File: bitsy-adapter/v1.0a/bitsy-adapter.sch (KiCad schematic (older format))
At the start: 17 parts, among them J1 PMOD1A, J2 PMOD1A, J3 PMOD1A, J4 5V AUX, J5 5V AUX, J6 5V AUX

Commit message: Finish bitsy-adapter v1.0a
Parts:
- removed J5: 5V AUX, Connector_PinSocket_2.54mm:PinSocket_2x01_P2.54mm_Vertical, symbol Connector_Generic:Conn_02x01
- added J6: IO3, pkl_pin_headers:Pin_Header_Straight_Round_1x01, symbol Connector_Generic:Conn_01x01
- added J7: IO2, pkl_pin_headers:Pin_Header_Straight_Round_1x01, symbol Connector_Generic:Conn_01x01
- added LOGO1: 1BitSquared, pkl_logos:1b2_Logo_SilkS_4mm, symbol pkl_logos:1BitSquared
- renumbered J6 to J5
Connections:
- net labels added: IO2, IO3
- wire segments 100 -> 102
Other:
- moved on the sheet: H1, H2, H3, H4, J1, J2, J3, J4, J5, R1A, R1B, R1C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

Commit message: Change bitsy adapter pinout
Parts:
- J2: value PMOD1A -> PMOD1B
- J3: value PMOD1A -> PMOD2
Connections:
- net labels added: P0, P1, P10, P11, P12, P13, P14, P15, P16, P17, P18, P19, P2, P20, P21, P22, P23, P3, P4, P5, P6, P7, P8, P9
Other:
- moved on the sheet: R1A, R1B, R1C, R1D, R2A, R2B, R2C, R2D, R3A, R3B, R3C, R3D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

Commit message: Bitsy Adapter: Remove unused IO2 & IO3 pins
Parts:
- removed J6: IO3, pkl_pin_headers:Pin_Header_Straight_Round_1x01, symbol Connector_Generic:Conn_01x01
- removed J7: IO2, pkl_pin_headers:Pin_Header_Straight_Round_1x01, symbol Connector_Generic:Conn_01x01
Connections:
- net labels removed: IO2, IO3
- wire segments 102 -> 100
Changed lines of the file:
@@
 $EndComp
-$Comp
-L Connector_Generic:Conn_01x01 J6
-U 1 1 5F3ED57C
-P 5800 5000
-F 0 "J6" H 5880 5042 50  0000 L CNN
-F 1 "IO3" H 5880 4951 50  0000 L CNN
-F 2 "pkl_pin_headers:Pin_Header_Straight_Round_1x01" H 5800 5000 50  0001 C CNN
-F 3 "~" H 5800 5000 50  0001 C CNN
-	1    5800 5000
-	1    0    0    -1
-$EndComp
-$Comp
-L Connector_Generic:Conn_01x01 J7
-U 1 1 5F3F0966
-P 5800 5200
-F 0 "J7" H 5880 5242 50  0000 L CNN
-F 1 "IO2" H 5880 5151 50  0000 L CNN
-F 2 "pkl_pin_headers:Pin_Header_Straight_Round_1x01" H 5800 5200 50  0001 C CNN
-F 3 "~" H 5800 5200 50  0001 C CNN
-	1    5800 5200
-	1    0    0    -1
-$EndComp
-Wire Wire Line
-	5600 5000 5300 5000
-Wire Wire Line
-	5600 5200 5300 5200
-Text Label 5300 5000 0    50   ~ 0
-IO3
-Text Label 5300 5200 0    50   ~ 0
-IO2
 $Comp
 L pkl_logos:1BitSquared LOGO1

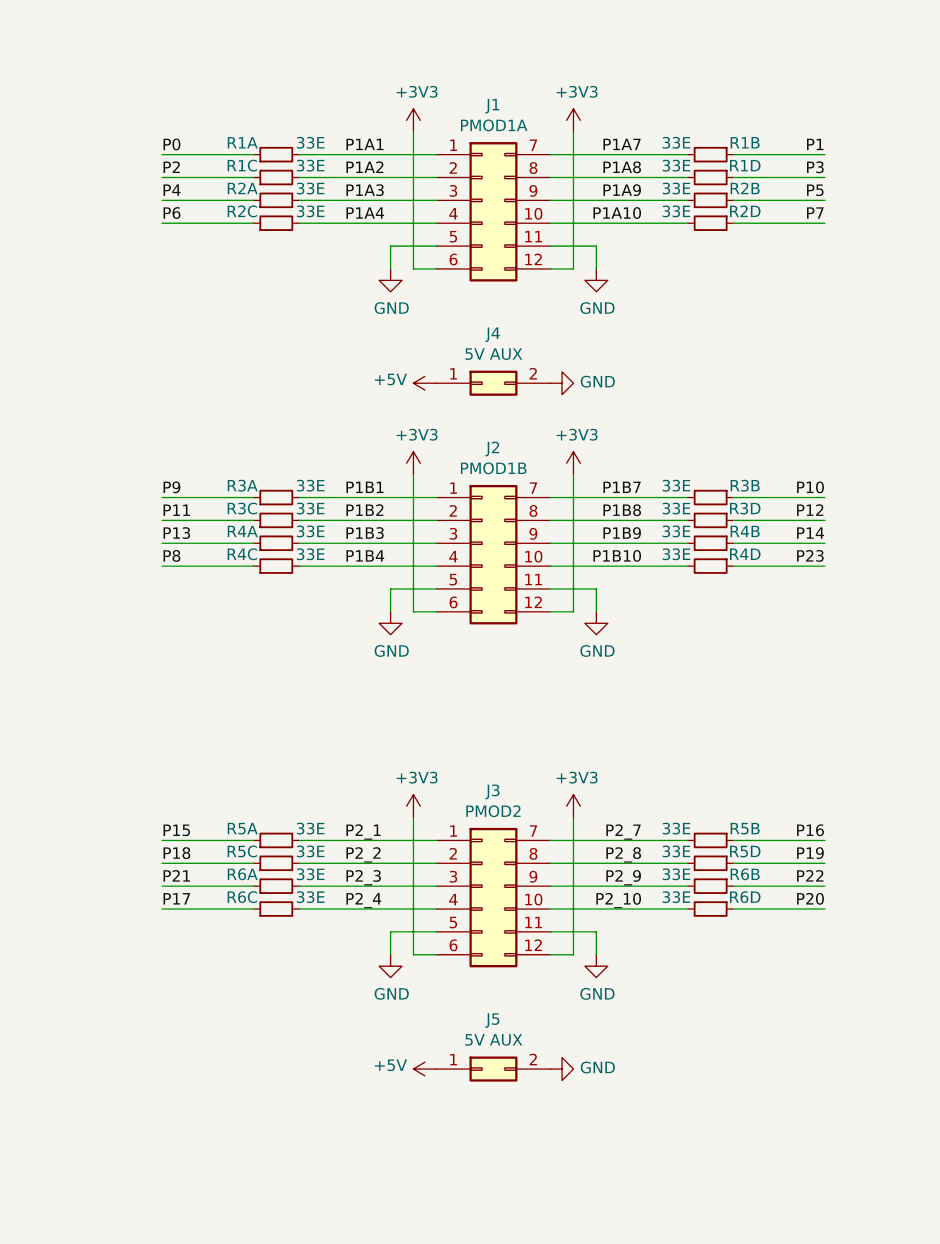
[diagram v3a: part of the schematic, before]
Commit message: Bitsy Adapter: Completely change pinout/formfactor
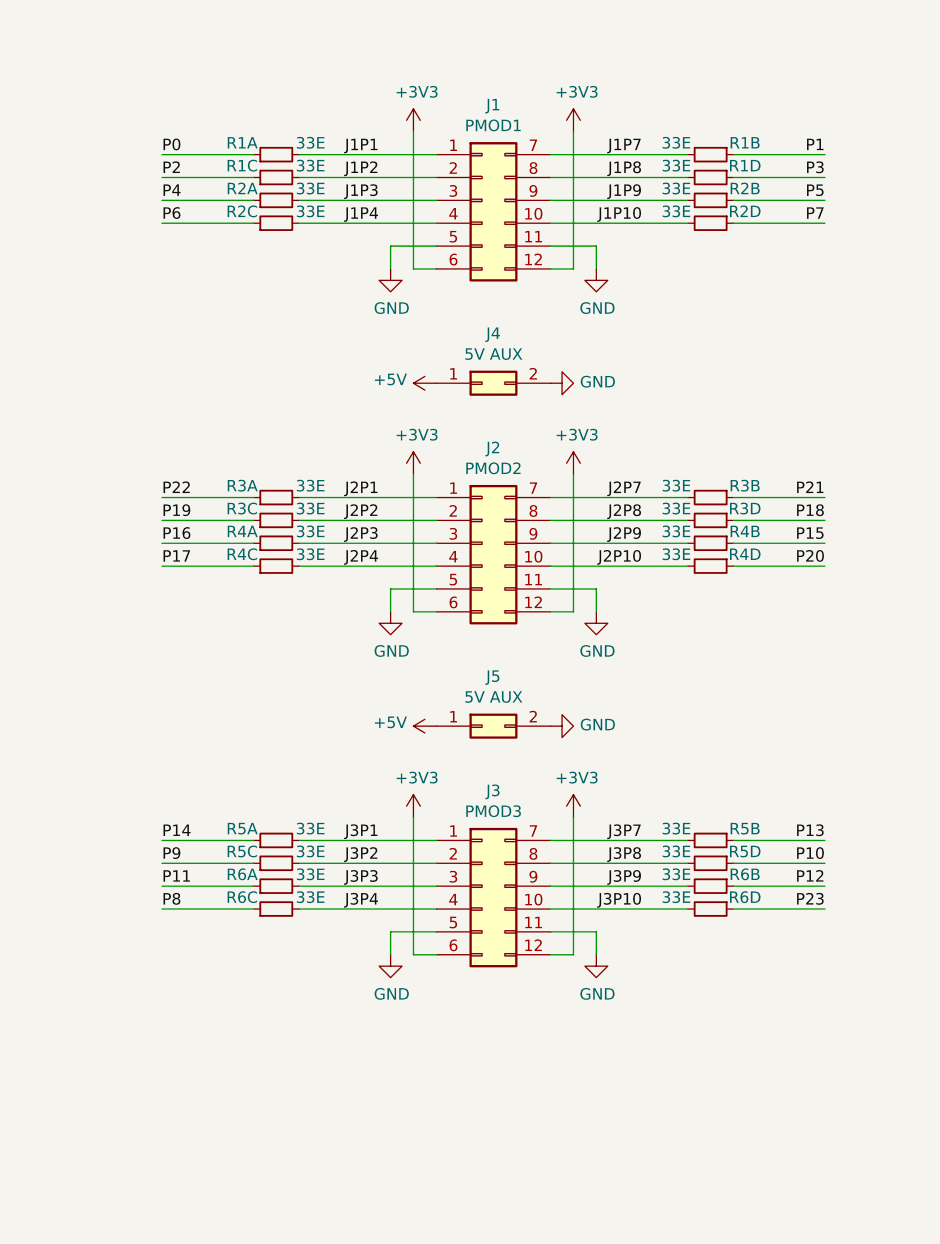
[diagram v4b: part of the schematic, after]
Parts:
- J1: value PMOD1A -> PMOD1
- J2: value PMOD1B -> PMOD2
- J3: value PMOD2 -> PMOD3
- LOGO1: footprint pkl_logos:1b2_Logo_SilkS_4mm -> pkl_logos:1b2_Logo_SilkS_6.5mm
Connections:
- net P10: now also R5.7; no longer R3.3
- net P11: now also R6.1; no longer R3.5
- net P12: now also R6.3; no longer R3.7
- net P13: now also R5.3; no longer R4.1
- net P14: now also R5.1; no longer R4.3
- net P15: now also R4.3; no longer R5.1
- net P16: now also R4.1; no longer R5.3
- net P17: now also R4.5; no longer R6.5
- net P18: now also R3.7; no longer R5.5
- net P19: now also R3.5; no longer R5.7
- net P20: now also R4.7; no longer R6.7
- net P21: now also R3.3; no longer R6.1
- net P22: now also R3.1; no longer R6.3
- net P23: now also R6.7; no longer R4.7
- net P8: now also R6.5; no longer R4.5
- net P9: now also R5.5; no longer R3.1
- net P1A1 renamed J1P1
- net P1A10 renamed J1P10
- net P1A2 renamed J1P2
- net P1A3 renamed J1P3
- net P1A4 renamed J1P4
- net P1A7 renamed J1P7
- net P1A8 renamed J1P8
- net P1A9 renamed J1P9
- net P1B1 renamed J2P1
- net P1B10 renamed J2P10
- net P1B2 renamed J2P2
- net P1B3 renamed J2P3
- net P1B4 renamed J2P4
- net P1B7 renamed J2P7
- net P1B8 renamed J2P8
- net P1B9 renamed J2P9
- net P2_1 renamed J3P1
- net P2_10 renamed J3P10
- net P2_2 renamed J3P2
- net P2_3 renamed J3P3
- net P2_4 renamed J3P4
- net P2_7 renamed J3P7
- net P2_8 renamed J3P8
- net P2_9 renamed J3P9
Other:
- moved on the sheet: J5
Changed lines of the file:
@@
 P 9200 2200
 F 0 "J1" H 9250 2617 50  0000 C CNN
-F 1 "PMOD1A" H 9250 2526 50  0000 C CNN
+F 1 "PMOD1" H 9250 2526 50  0000 C CNN
 F 2 "pkl_pin_headers:PinSocket_2x06_P2.54mm_Horizontal_Top_Bottom" H 9200 2200 50  0001 C CNN
 F 3 "~" H 9200 2200 50  0001 C CNN
@@
 	9500 3600 10100 3600
 Wire Wire Line
+	10300 5100 10700 5100
+Text Label 10700 5100 2    50   ~ 0
+P10
+Wire Wire Line
+	9500 3700 10100 3700
+Wire Wire Line
+	9500 3800 10100 3800
+Wire Wire Line
+	10300 5300 10700 5300
+Text Label 10700 5300 2    50   ~ 0
+P23
+Wire Wire Line
+	9500 5000 10100 5000
+Wire Wire Line
+	9500 5100 10100 5100
+Wire Wire Line
+	10300 3700 10700 3700
+Wire Wire Line
+	10300 3600 10700 3600
+Text Label 10700 3700 2    50   ~ 0
+P15
+Text Label 10700 3600 2    50   ~ 0
+P18
+Wire Wire Line
+	9500 5200 10100 5200
+Wire Wire Line
+	9500 5300 10100 5300
+Wire Wire Line
 	10300 3500 10700 3500
 Wire Wire Line
-	10300 3600 10700 3600
+	10300 3800 10700 3800
 Text Label 10700 3500 2    50   ~ 0
-P10
-Text Label 10700 3600 2    50   ~ 0
-P12
-Wire Wire Line
-	9500 3700 10100 3700
-Wire Wire Line
-	9500 3800 10100 3800
-Wire Wire Line
-	10300 3700 10700 3700
-Wire Wire Line
-	10300 3800 10700 3800
-Text Label 10700 3700 2    50   ~ 0
-P14
+P21
 Text Label 10700 3800 2    50   ~ 0
-P23
-Wire Wire Line
-	9500 5000 10100 5000
-Wire Wire Line
-	9500 5100 10100 5100
-Wire Wire Line
-	10300 5000 10700 5000
-Wire Wire Line
-	10300 5100 10700 5100
-Text Label 10700 5000 2    50   ~ 0
-P16
-Text Label 10700 5100 2    50   ~ 0
-P19
-Wire Wire Line
-	9500 5200 10100 5200
-Wire Wire Line
-	9500 5300 10100 5300
-Wire Wire Line
-	10300 5200 10700 5200
-Wire Wire Line
-	10300 5300 10700 5300
-Text Label 10700 5200 2    50   ~ 0
-P22
-Text Label 10700 5300 2    50   ~ 0
 P20
 $Comp
@@
 L power:+5V #PWR0115
 U 1 1 5F432D28
-P 9000 6000
-F 0 "#PWR0115" H 9000 5850 50  0001 C CNN
-F 1 "+5V" V 9015 6128 50  0000 L CNN
-F 2 "" H 9000 6000 50  0001 C CNN
-F 3 "" H 9000 6000 50  0001 C CNN
-	1    9000 6000
+P 9000 4500
+F 0 "#PWR0115" H 9000 4350 50  0001 C CNN
+F 1 "+5V" V 9015 4628 50  0000 L CNN
+F 2 "" H 9000 4500 50  0001 C CNN
+F 3 "" H 9000 4500 50  0001 C CNN
+	1    9000 4500
 	0    -1   -1   0
 $EndComp
@@
 L power:GND #PWR0116
 U 1 1 5F432D32
-P 9500 6000
-F 0 "#PWR0116" H 9500 5750 50  0001 C CNN
-F 1 "GND" V 9505 5872 50  0000 R CNN
-F 2 "" H 9500 6000 50  0001 C CNN
-F 3 "" H 9500 6000 50  0001 C CNN
-	1    9500 6000
+P 9500 4500
+F 0 "#PWR0116" H 9500 4250 50  0001 C CNN
+F 1 "GND" V 9505 4372 50  0000 R CNN
+F 2 "" H 9500 4500 50  0001 C CNN
+F 3 "" H 9500 4500 50  0001 C CNN
+	1    9500 4500
 	0    -1   -1   0
 $EndComp
@@
 L Connector_Generic:Conn_02x01 J5
 U 1 1 5F432D3C
-P 9200 6000
-F 0 "J5" H 9250 6217 50  0000 C CNN
-F 1 "5V AUX" H 9250 6126 50  0000 C CNN
-F 2 "Connector_PinSocket_2.54mm:PinSocket_2x01_P2.54mm_Vertical" H 9200 6000 50  0001 C CNN
-F 3 "~" H 9200 6000 50  0001 C CNN
-	1    9200 6000
+P 9200 4500
+F 0 "J5" H 9250 4717 50  0000 C CNN
+F 1 "5V AUX" H 9250 4626 50  0000 C CNN
+F 2 "Connector_PinSocket_2.54mm:PinSocket_2x01_P2.54mm_Vertical" H 9200 4500 50  0001 C CNN
+F 3 "~" H 9200 4500 50  0001 C CNN
+	1    9200 4500
 	1    0    0    -1
 $EndComp
@@
 P 9200 3700
 F 0 "J2" H 9250 4117 50  0000 C CNN
-F 1 "PMOD1B" H 9250 4026 50  0000 C CNN
+F 1 "PMOD2" H 9250 4026 50  0000 C CNN
 F 2 "pkl_pin_headers:PinSocket_2x06_P2.54mm_Horizontal_Top_Bottom" H 9200 3700 50  0001 C CNN
 F 3 "~" H 9200 3700 50  0001 C CNN
@@
 P 9200 5200
 F 0 "J3" H 9250 5617 50  0000 C CNN
-F 1 "PMOD2" H 9250 5526 50  0000 C CNN
+F 1 "PMOD3" H 9250 5526 50  0000 C CNN
 F 2 "pkl_pin_headers:PinSocket_2x06_P2.54mm_Horizontal_Top_Bottom" H 9200 5200 50  0001 C CNN
 F 3 "~" H 9200 5200 50  0001 C CNN
@@
 F 0 "LOGO1" V 11200 6975 60  0001 C CNN
 F 1 "1BitSquared" H 11153 6950 40  0001 L CNN
-F 2 "pkl_logos:1b2_Logo_SilkS_4mm" H 11000 6950 60  0001 C CNN
+F 2 "pkl_logos:1b2_Logo_SilkS_6.5mm" H 11000 6950 60  0001 C CNN
 F 3 "" H 11000 6950 60  0000 C CNN
 	1    11000 6950
@@
 	1    0    0    -1
 $EndComp
-Text Label 7800 5300 0    50   ~ 0
+Text Label 7800 3800 0    50   ~ 0
 P17
+Wire Wire Line
+	8200 3800 7800 3800
+Wire Wire Line
+	8200 3500 7800 3500
+Text Label 7800 3600 0    50   ~ 0
+P19
+Text Label 7800 3700 0    50   ~ 0
+P16
+Wire Wire Line
+	8200 3600 7800 3600
+Wire Wire Line
+	8200 3700 7800 3700
+Text Label 7800 5000 0    50   ~ 0
+P14
+Wire Wire Line
+	8200 5300 7800 5300
+Wire Wire Line
+	8200 5000 7800 5000
+Wire Wire Line
+	8400 3800 9000 3800
+Wire Wire Line
+	8400 3700 9000 3700
 Text Label 7800 5200 0    50   ~ 0
-P21
-Wire Wire Line
-	8200 5300 7800 5300
+P11
+Text Label 7800 5100 0    50   ~ 0
+P9
 Wire Wire Line
 	8200 5200 7800 5200
-Text Label 7800 5100 0    50   ~ 0
-P18
-Text Label 7800 5000 0    50   ~ 0
-P15
 Wire Wire Line
 	8200 5100 7800 5100
-Wire Wire Line
-	8200 5000 7800 5000
-Text Label 7800 3700 0    50   ~ 0
-P13
-Wire Wire Line
-	8200 3800 7800 3800
-Wire Wire Line
-	8200 3700 7800 3700
-Wire Wire Line
-	8400 3800 9000 3800
-Wire Wire Line
-	8400 3700 9000 3700
-Text Label 7800 3600 0    50   ~ 0
-P11
-Text Label 7800 3500 0    50   ~ 0
-P9
-Wire Wire Line
-	8200 3600 7800 3600
-Wire Wire Line
-	8200 3500 7800 3500
 Wire Wire Line
 	8400 3600 9000 3600
@@
 	0    -1   -1   0
 $EndComp
-Text Label 8600 2000 0    50   ~ 0
-P1A1
-Text Label 8600 2100 0    50   ~ 0
-P1A2
-Text Label 8600 2200 0    50   ~ 0
-P1A3
-Text Label 8600 2300 0    50   ~ 0
-P1A4
-Text Label 9900 2000 2    50   ~ 0
-P1A7
-Text Label 9900 2100 2    50   ~ 0
-P1A8
-Text Label 9900 2200 2    50   ~ 0
-P1A9
-Text Label 9900 2300 2    50   ~ 0
-P1A10
 Text Label 8600 3800 0    50   ~ 0
-P1B4
+J2P4
 Text Label 8600 3700 0    50   ~ 0
-P1B3
+J2P3
 Text Label 8600 3600 0    50   ~ 0
-P1B2
+J2P2
 Text Label 8600 3500 0    50   ~ 0
-P1B1
+J2P1
 Wire Wire Line
 	8400 5000 9000 5000
@@
 	8400 5300 9000 5300
 Text Label 9900 3500 2    50   ~ 0
-P1B7
+J2P7
 Text Label 9900 3600 2    50   ~ 0
-P1B8
+J2P8
 Text Label 9900 3700 2    50   ~ 0
-P1B9
+J2P9
 Text Label 9900 3800 2    50   ~ 0
-P1B10
+J2P10
 Text Label 8600 5000 0    50   ~ 0
-P2_1
+J3P1
 Text Label 8600 5100 0    50   ~ 0
-P2_2
+J3P2
 Text Label 8600 5200 0    50   ~ 0
-P2_3
+J3P3
 Text Label 8600 5300 0    50   ~ 0
-P2_4
+J3P4
 Text Label 9900 5000 2    50   ~ 0
-P2_7
+J3P7
 Text Label 9900 5100 2    50   ~ 0
-P2_8
+J3P8
 Text Label 9900 5200 2    50   ~ 0
-P2_9
+J3P9
 Text Label 9900 5300 2    50   ~ 0
-P2_10
-Text Label 7800 3800 0    50   ~ 0
+J3P10
+Text Label 7800 5300 0    50   ~ 0
 P8
+Text Label 7800 3500 0    50   ~ 0
+P22
+Text Label 9900 2000 2    50   ~ 0
+J1P7
+Text Label 9900 2100 2    50   ~ 0
+J1P8
+Text Label 9900 2200 2    50   ~ 0
+J1P9
+Text Label 9900 2300 2    50   ~ 0
+J1P10
+Text Label 8600 2300 0    50   ~ 0
+J1P4
+Text Label 8600 2200 0    50   ~ 0
+J1P3
+Text Label 8600 2100 0    50   ~ 0
+J1P2
+Text Label 8600 2000 0    50   ~ 0
+J1P1
+Text Label 10700 5000 2    50   ~ 0
+P13
+Wire Wire Line
+	10300 5000 10700 5000
+Text Label 10700 5200 2    50   ~ 0
+P12
+Wire Wire Line
+	10300 5200 10700 5200
 $EndSCHEMATC

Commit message: Bitsy Adapter: finish v1.0a
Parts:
- added FID1, FID2, FID3: Fiducial, Fiducial:Fiducial_0.5mm_Mask1.5mm, symbol Mechanical:Fiducial
- added JP1: CRESET, Connector_PinHeader_2.54mm:PinHeader_1x02_P2.54mm_Vertical, symbol Jumper:Jumper_2_Open
- LOGO1: footprint pkl_logos:1b2_Logo_SilkS_6.5mm -> pkl_logos:1b2_Logo_SilkS_7.5mm
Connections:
- net labels added: CDONE, CRESET
- wire segments 100 -> 110

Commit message: Bitsy Adapter: finish v1.0a for real this time
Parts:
- added unit 2 of A1
- added unit 3 of A1
- LOGO1: footprint pkl_logos:1b2_Logo_SilkS_7.5mm -> pkl_logos:1b2_Logo_SilkS_6.5mm
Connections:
- net labels added: SPI_CIPO, SPI_COPI, SPI_CS, SPI_SCK
- wire segments 110 -> 102

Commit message: Bitsy Adapter: increase board size to accomadate better grounding
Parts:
- added C1, C2, C3: 1u, pkl_dipol:C_0603, symbol Device:C_Small
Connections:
- no-connect marks 0 -> 1
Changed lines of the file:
@@
 Sheet 1 1
 Title "iCEBreaker Bitsy PMOD Adapter"
-Date "2020-10-30"
+Date "2020-11-01"
 Rev "v1.0a"
 Comp "1BitSquared"
@@
 $EndComp
 $Comp
-L power:+3.3V #PWR?
-U 1 1 5FA27AC9
-P 6300 4200
-F 0 "#PWR?" H 6300 4050 50  0001 C CNN
-F 1 "+3.3V" V 6315 4328 50  0000 L CNN
-F 2 "" H 6300 4200 50  0001 C CNN
-F 3 "" H 6300 4200 50  0001 C CNN
-	1    6300 4200
-	0    1    -1   0
-$EndComp
-$Comp
-L power:GND #PWR?
+L power:GND #PWR0122
 U 1 1 5FA280F2
 P 6300 4100
-F 0 "#PWR?" H 6300 3850 50  0001 C CNN
+F 0 "#PWR0122" H 6300 3850 50  0001 C CNN
 F 1 "GND" V 6305 3972 50  0000 R CNN
 F 2 "" H 6300 4100 50  0001 C CNN
@@
 $EndComp
 $Comp
-L power:GND #PWR?
+L power:GND #PWR0123
 U 1 1 5FA693AF
 P 7100 4000
-F 0 "#PWR?" H 7100 3750 50  0001 C CNN
+F 0 "#PWR0123" H 7100 3750 50  0001 C CNN
 F 1 "GND" V 7105 3872 50  0000 R CNN
 F 2 "" H 7100 4000 50  0001 C CNN
@@
 	0    1    -1   0
 $EndComp
+$Comp
+L Device:C_Small C1
+U 1 1 5F9E39BF
+P 10000 2800
+F 0 "C1" H 10092 2846 50  0000 L CNN
+F 1 "1u" H 10092 2755 50  0000 L CNN
+F 2 "pkl_dipol:C_0603" H 10000 2800 50  0001 C CNN
+F 3 "~" H 10000 2800 50  0001 C CNN
+	1    10000 2800
+	1    0    0    -1
+$EndComp
+$Comp
+L power:+3V3 #PWR0124
+U 1 1 5F9E4D6B
+P 10000 2700
+F 0 "#PWR0124" H 10000 2550 50  0001 C CNN
+F 1 "+3V3" H 10015 2873 50  0000 C CNN
+F 2 "" H 10000 2700 50  0001 C CNN
+F 3 "" H 10000 2700 50  0001 C CNN
+	1    10000 2700
+	1    0    0    -1
+$EndComp
+$Comp
+L power:GND #PWR0125
+U 1 1 5F9E5121
+P 10000 2900
+F 0 "#PWR0125" H 10000 2650 50  0001 C CNN
+F 1 "GND" H 10005 2727 50  0000 C CNN
+F 2 "" H 10000 2900 50  0001 C CNN
+F 3 "" H 10000 2900 50  0001 C CNN
+	1    10000 2900
+	1    0    0    -1
+$EndComp
+$Comp
+L Device:C_Small C2
+U 1 1 5F9EC5B0
+P 10000 4300
+F 0 "C2" H 10092 4346 50  0000 L CNN
+F 1 "1u" H 10092 4255 50  0000 L CNN
+F 2 "pkl_dipol:C_0603" H 10000 4300 50  0001 C CNN
+F 3 "~" H 10000 4300 50  0001 C CNN
+	1    10000 4300
+	1    0    0    -1
+$EndComp
+$Comp
+L power:+3V3 #PWR0126
+U 1 1 5F9EC5C8
+P 10000 4200
+F 0 "#PWR0126" H 10000 4050 50  0001 C CNN
+F 1 "+3V3" H 10015 4373 50  0000 C CNN
+F 2 "" H 10000 4200 50  0001 C CNN
+F 3 "" H 10000 4200 50  0001 C CNN
+	1    10000 4200
+	1    0    0    -1
+$EndComp
+$Comp
+L power:GND #PWR0127
+U 1 1 5F9EC5D2
+P 10000 4400
+F 0 "#PWR0127" H 10000 4150 50  0001 C CNN
+F 1 "GND" H 10005 4227 50  0000 C CNN
+F 2 "" H 10000 4400 50  0001 C CNN
+F 3 "" H 10000 4400 50  0001 C CNN
+	1    10000 4400
+	1    0    0    -1
+$EndComp
+$Comp
+L Device:C_Small C3
+U 1 1 5F9F7C33
+P 10000 5800
+F 0 "C3" H 10092 5846 50  0000 L CNN
+F 1 "1u" H 10092 5755 50  0000 L CNN
+F 2 "pkl_dipol:C_0603" H 10000 5800 50  0001 C CNN
+F 3 "~" H 10000 5800 50  0001 C CNN
+	1    10000 5800
+	1    0    0    -1
+$EndComp
+$Comp
+L power:+3V3 #PWR0128
+U 1 1 5F9F7C4B
+P 10000 5700
+F 0 "#PWR0128" H 10000 5550 50  0001 C CNN
+F 1 "+3V3" H 10015 5873 50  0000 C CNN
+F 2 "" H 10000 5700 50  0001 C CNN
+F 3 "" H 10000 5700 50  0001 C CNN
+	1    10000 5700
+	1    0    0    -1
+$EndComp
+$Comp
+L power:GND #PWR0129
+U 1 1 5F9F7C55
+P 10000 5900
+F 0 "#PWR0129" H 10000 5650 50  0001 C CNN
+F 1 "GND" H 10005 5727 50  0000 C CNN
+F 2 "" H 10000 5900 50  0001 C CNN
+F 3 "" H 10000 5900 50  0001 C CNN
+	1    10000 5900
+	1    0    0    -1
+$EndComp
+NoConn ~ 6300 4200
 $EndSCHEMATC
